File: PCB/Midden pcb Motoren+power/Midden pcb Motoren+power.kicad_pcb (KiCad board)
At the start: 2 copper layers, 232 parts, among them IC1 TB9051FTG, IC2 TB9051FTG, IC3 TB9051FTG, IC4 TB9051FTG, J4 Conn_01x08_Socket, J5 Conn_01x03_Socket, J6 Conn_01x08_Socket, J7 Conn_01x08_Pin, J8 Conn_01x03_Pin, SW10 SW_DIP_x04, SW5 SW_DIP_x03, SW6 SW_DPST_x2, SW7 SW_DIP_x04, SW8 SW_DIP_x04, SW9 SW_DIP_x04, U10 FT232RL, U11 ATmega328P-M, U12 ATmega328P-M, U13 FT232RL, U14 FT232RL, U6 ATmega328P-M, U7 ATmega328P-M, U9 FT232RL

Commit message: M1 is af
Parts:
- removed J5: Conn_01x03_Socket, Connector_JST:JST_EH_S3B-EH_1x03_P2.50mm_Horizontal
- removed J8: Conn_01x03_Pin, Connector_JST:JST_EH_S3B-EH_1x03_P2.50mm_Horizontal
- added J1: Conn_01x04_Pin, Connector_JST:JST_EH_S4B-EH_1x04_P2.50mm_Horizontal, F.Cu at (156.1, 132.2)
- added J2: Conn_01x04_Socket, Connector_JST:JST_EH_S4B-EH_1x04_P2.50mm_Horizontal, F.Cu at (98.5, 94.6)
- added J3: Conn_01x08_Socket, Connector_JST:JST_EH_S8B-EH_1x08_P2.50mm_Horizontal, F.Cu at (156.0, 145.8)
- C106, C83, C85, C86, C87, C97, C98, R101, R104, R109, R110, R111, R119, R120, R169, R170, R171, R172, R173, R174, R175, R176, R177, R205, R206, R207, R219, R220, R94, R95, R96, U6, U9: moved to B.Cu
- moved SW10 179.3 mm to (78.8, 118.8), turned to 120 degrees
- moved C98 156.8 mm to (125.3, 68.0)
- moved C97 156.7 mm to (125.3, 67.3)
- moved SW9 155.6 mm to (90.1, 112.2), turned to 120 degrees
- moved C87 151.1 mm to (125.5, 66.1), turned to 180 degrees
- moved C86 151.0 mm to (125.5, 65.4), turned to 180 degrees
- moved C85 151.0 mm to (125.5, 64.6)
- moved R219 147.4 mm to (115.3, 67.0)
- moved U6 146.3 mm to (121.2, 65.6), turned to 180 degrees
- moved R220 146.3 mm to (115.8, 64.0)
- moved M4 146.0 mm to (73.3, 127.1), turned to 30 degrees
- moved R170 132.8 mm to (118.1, 71.0), turned to 90 degrees
- moved R169 131.8 mm to (119.6, 70.9), turned to 90 degrees
- moved R171 131.4 mm to (117.7, 60.7), turned to -90 degrees
- moved R205 130.9 mm to (129.4, 81.8)
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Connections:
- net /12V renamed +12V
- 3V1 pad 1: GND -> /3V3
- 5V1 pad 1: GND -> /5V
- J6 pad 1: GND -> unconnected-(J6-Pin_1-Pad1)
- J6 pad 2: GND -> unconnected-(J6-Pin_2-Pad2)
- J6 pad 3: GND -> /SCL
- J6 pad 4: GND -> /SDA
- J6 pad 5: GND -> /LED
- J6 pad 6: GND -> /5V
- J6 pad 8: GND -> /3V3
- JP28 pad 2: GND -> /SCL
- JP29 pad 2: GND -> /SDA
- R125 pad 2: GND -> /SDA
- R126 pad 2: GND -> /SCL
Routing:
- net +5V: track 0.00 -> 93.0 mm, vias 0 -> 4
- net Net-(R95-Pad2): track 0.00 -> 50.6 mm, vias 0 -> 2
- net Net-(R94-Pad2): track 0.00 -> 47.7 mm, vias 0 -> 2
- net /tx-m1: track 0.00 -> 47.5 mm
- net /tx-m10: track 0.00 -> 44.0 mm, vias 0 -> 1
- net /out2-m1: track 0.00 -> 42.1 mm
- net /out1-m1: track 0.00 -> 41.4 mm
- net /rx-m1: track 0.00 -> 40.9 mm
- net /rx-m10: track 0.00 -> 36.7 mm, vias 0 -> 1
- net /enAM1: track 0.00 -> 23.0 mm, vias 0 -> 2
- net /ocm-m1: track 0.00 -> 21.4 mm, vias 0 -> 2
- net /encB-m1: track 0.00 -> 18.5 mm
- net /encA-m1: track 0.00 -> 17.8 mm, vias 0 -> 1
- net /pwm1-m1: track 0.00 -> 13.9 mm, vias 0 -> 3
- net /occ-m1: track 0.00 -> 13.7 mm, vias 0 -> 2
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- added copper zone on B.Cu, net GND
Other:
- board outline added: 153.6 x 125.2 mm

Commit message: v1
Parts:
- moved C115 10.9 mm to (212.5, 56.0)
- moved C133 10.9 mm to (216.8, 56.0)
- moved C91 10.9 mm to (273.7, 60.6)
- moved C92 10.9 mm to (273.7, 62.4)
- moved R114 10.9 mm to (225.5, 56.0)
- moved R146 10.9 mm to (234.2, 56.0)
- moved R162 10.9 mm to (238.6, 56.0)
- moved R178 10.9 mm to (242.9, 56.0)
- moved R194 10.9 mm to (247.3, 56.0)
- moved R210 10.9 mm to (251.6, 56.0)
- moved R98 10.9 mm to (221.2, 56.0)
- moved 5V1 10.9 mm to (196.3, 83.1)
- moved BT1 10.9 mm to (174.0, 112.7)
- moved BT2 10.9 mm to (168.1, 101.7)
- moved C100 10.9 mm to (276.5, 64.2)
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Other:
- board size 153.6 x 125.2 mm -> 148.1 x 115.8 mm

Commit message: m2
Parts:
- C100, C101, R106, R112, R113, R114, R187, R188, R189, R190, R191, R192, R193, R194, R195, R98, R99, U7: moved to B.Cu
- moved C100 152.9 mm to (127.4, 97.9)
- moved C101 152.7 mm to (127.4, 98.7)
- moved R188 142.8 mm to (118.4, 102.6), turned to 90 degrees
- moved R187 142.6 mm to (119.9, 102.6), turned to 90 degrees
- moved R189 138.0 mm to (117.7, 90.8), turned to -90 degrees
- moved R190 135.7 mm to (119.2, 90.8), turned to -90 degrees
- moved U7 135.7 mm to (122.6, 96.9), turned to 180 degrees
- moved R191 133.5 mm to (120.7, 90.8), turned to -90 degrees
- moved R195 129.1 mm to (125.9, 102.6), turned to 90 degrees
- moved R192 126.6 mm to (127.6, 92.5), turned to 180 degrees
- moved R193 126.3 mm to (127.6, 94.0), turned to 180 degrees
- moved R194 126.0 mm to (127.6, 95.6), turned to 180 degrees
- moved R106 117.0 mm to (122.2, 90.8), turned to 90 degrees
- moved R113 115.1 mm to (121.4, 102.6), turned to -90 degrees
- moved R112 113.5 mm to (124.4, 102.6), turned to -90 degrees
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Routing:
- net Net-(R98-Pad2): track 0.00 -> 50.6 mm
- net Net-(R99-Pad2): track 0.00 -> 48.1 mm
- net /out1-m3: track 0.00 -> 45.9 mm
- net /out2-m3: track 0.00 -> 27.5 mm
- net /encB-m3: track 0.00 -> 18.8 mm, vias 0 -> 1
- net /encA-m3: track 0.00 -> 17.6 mm, vias 0 -> 1
- net Net-(IC2-ENB): track 0.00 -> 17.6 mm, vias 0 -> 1
- net GND: track 0.00 -> 16.3 mm
- net Net-(IC2-OCC): track 0.00 -> 16.3 mm, vias 0 -> 1
- net Net-(IC2-EN): track 0.00 -> 12.0 mm
- net /pwm1-m3: track 0.00 -> 9.12 mm
- net Net-(U7-PC3): track 0.00 -> 5.20 mm
- net Net-(U7-PC4): track 0.00 -> 4.32 mm
- net Net-(U7-PD7): track 0.00 -> 4.01 mm
- net Net-(U7-PB4): track 0.00 -> 3.70 mm
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
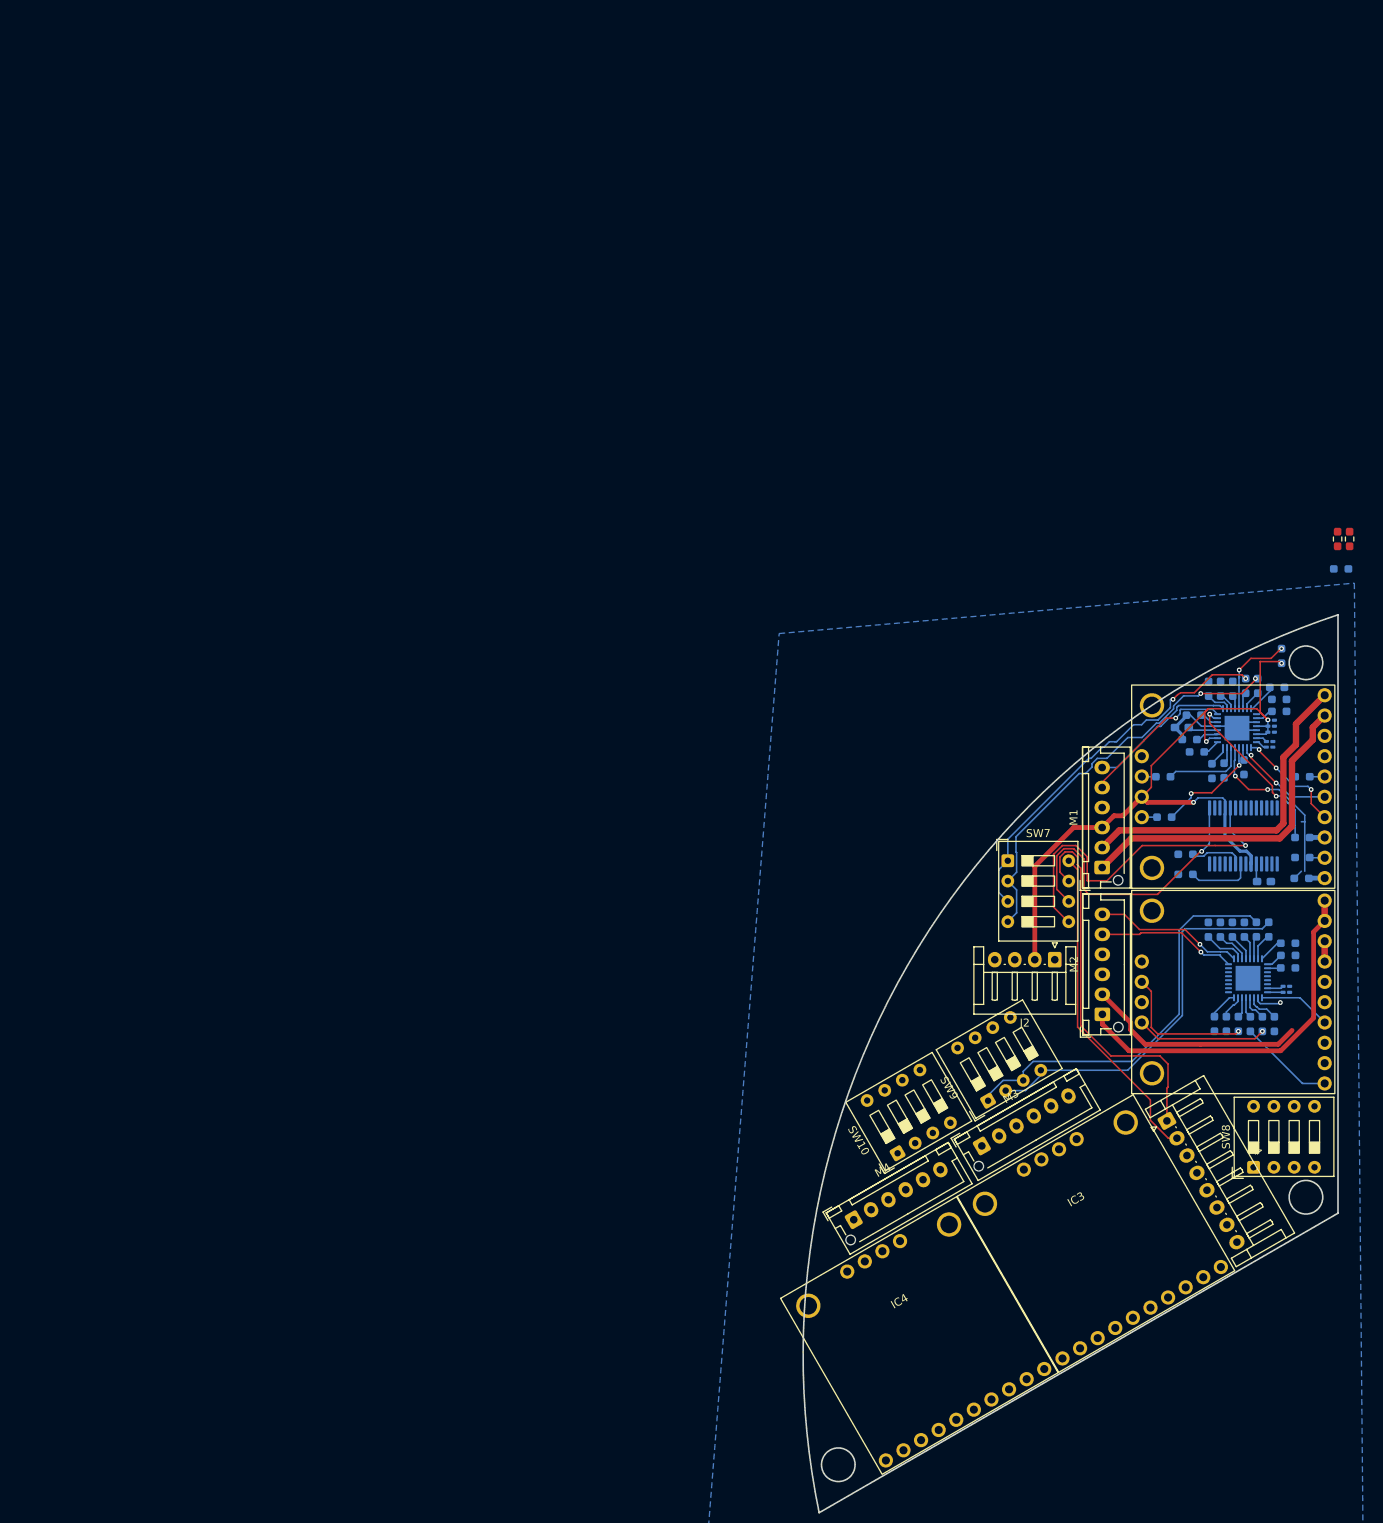
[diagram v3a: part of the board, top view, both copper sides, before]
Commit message: motor driver symbol changed
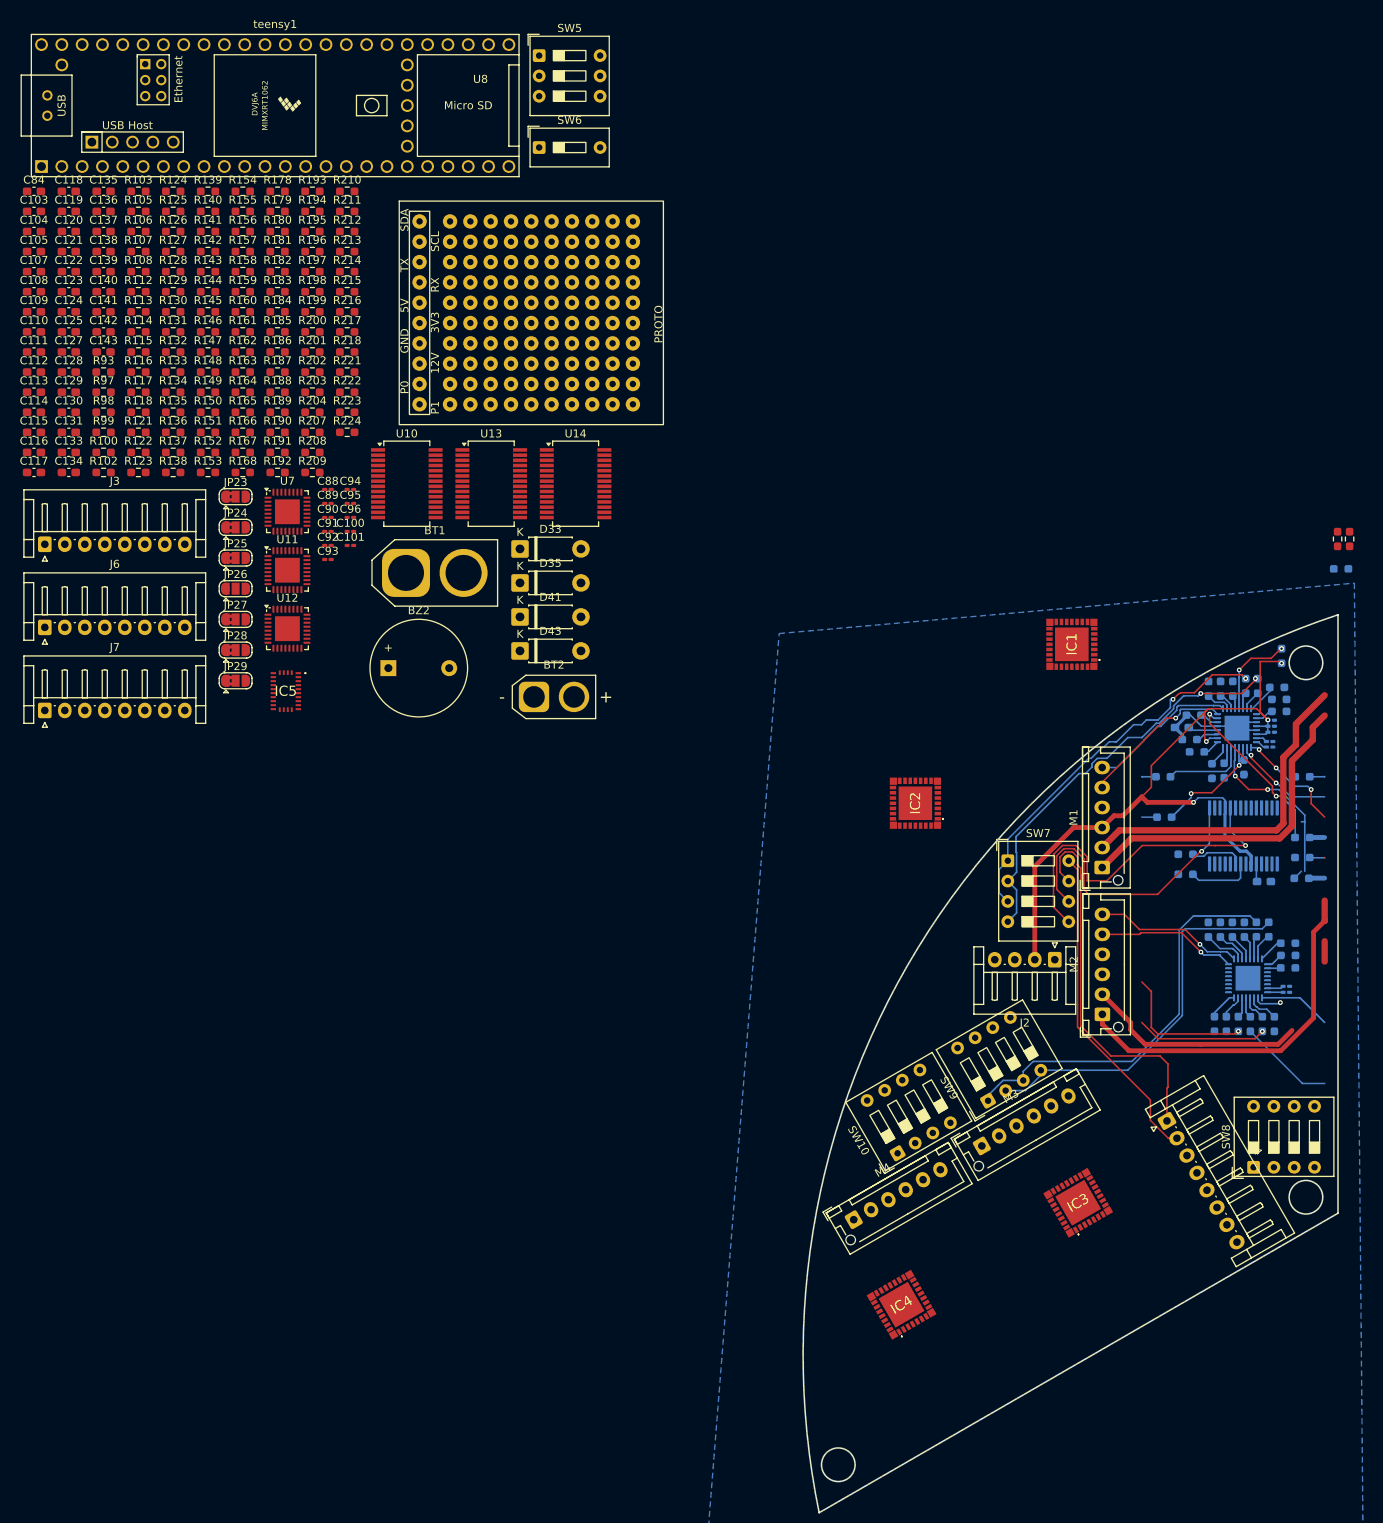
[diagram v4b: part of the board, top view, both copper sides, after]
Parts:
- added BT1: Battery, Connector_AMASS:AMASS_XT60-F_1x02_P7.20mm_Vertical, F.Cu at (17.4, 46.2)
- added BT2: Battery, Connector_AMASS:AMASS_XT30U-M_1x02_P5.0mm_Vertical, F.Cu at (33.4, 61.7)
- added BZ2: Buzzer, Buzzer_Beeper:Buzzer_12x9.5RM7.6, F.Cu at (15.2, 58.1)
- added C100: 20pF???, Capacitor_SMD:C_0201_0603Metric_Pad0.64x0.40mm_HandSolder, F.Cu at (10.4, 41.0)
- added C101: 20pF???, Capacitor_SMD:C_0201_0603Metric_Pad0.64x0.40mm_HandSolder, F.Cu at (10.4, 42.8)
- added C103: 47uF, Capacitor_SMD:C_0603_1608Metric_Pad1.08x0.95mm_HandSolder, F.Cu at (-29.1, 1.03)
- added C104: 47uF, Capacitor_SMD:C_0603_1608Metric_Pad1.08x0.95mm_HandSolder, F.Cu at (-29.1, 3.54)
- added C105: 0.1uF, Capacitor_SMD:C_0603_1608Metric_Pad1.08x0.95mm_HandSolder, F.Cu at (-29.1, 6.05)
- added C107: 0.1uF, Capacitor_SMD:C_0603_1608Metric_Pad1.08x0.95mm_HandSolder, F.Cu at (-29.1, 8.56)
- added C108: 0.1uF, Capacitor_SMD:C_0603_1608Metric_Pad1.08x0.95mm_HandSolder, F.Cu at (-29.1, 11.1)
- added C109: 100nF, Capacitor_SMD:C_0603_1608Metric_Pad1.08x0.95mm_HandSolder, F.Cu at (-29.1, 13.6)
- added C110: 0.1uF, Capacitor_SMD:C_0603_1608Metric_Pad1.08x0.95mm_HandSolder, F.Cu at (-29.1, 16.1)
- added C111: 100nF, Capacitor_SMD:C_0603_1608Metric_Pad1.08x0.95mm_HandSolder, F.Cu at (-29.1, 18.6)
- added C112: 4.7uF, Capacitor_SMD:C_0603_1608Metric_Pad1.08x0.95mm_HandSolder, F.Cu at (-29.1, 21.1)
- added C113: 1uF, Capacitor_SMD:C_0603_1608Metric_Pad1.08x0.95mm_HandSolder, F.Cu at (-29.1, 23.6)
- added C114: 1uF, Capacitor_SMD:C_0603_1608Metric_Pad1.08x0.95mm_HandSolder, F.Cu at (-29.1, 26.1)
- added C115: 100nF, Capacitor_SMD:C_0603_1608Metric_Pad1.08x0.95mm_HandSolder, F.Cu at (-29.1, 28.6)
- added C116: 0.1uF, Capacitor_SMD:C_0603_1608Metric_Pad1.08x0.95mm_HandSolder, F.Cu at (-29.1, 31.2)
- added C117: 4.7uF, Capacitor_SMD:C_0603_1608Metric_Pad1.08x0.95mm_HandSolder, F.Cu at (-29.1, 33.7)
- added C118: 4.7uF, Capacitor_SMD:C_0603_1608Metric_Pad1.08x0.95mm_HandSolder, F.Cu at (-24.8, -1.48)
- added C119: 1uF, Capacitor_SMD:C_0603_1608Metric_Pad1.08x0.95mm_HandSolder, F.Cu at (-24.8, 1.03)
- added C120: 1uF, Capacitor_SMD:C_0603_1608Metric_Pad1.08x0.95mm_HandSolder, F.Cu at (-24.8, 3.54)
- added C121: 0.47uF, Capacitor_SMD:C_0603_1608Metric_Pad1.08x0.95mm_HandSolder, F.Cu at (-24.8, 6.05)
- added C122: 0.1uF, Capacitor_SMD:C_0603_1608Metric_Pad1.08x0.95mm_HandSolder, F.Cu at (-24.8, 8.56)
- added C123: 20pF???, Capacitor_SMD:C_0603_1608Metric_Pad1.08x0.95mm_HandSolder, F.Cu at (-24.8, 11.1)
- added C124: 20pF???, Capacitor_SMD:C_0603_1608Metric_Pad1.08x0.95mm_HandSolder, F.Cu at (-24.8, 13.6)
- added C125: 4.7uF, Capacitor_SMD:C_0603_1608Metric_Pad1.08x0.95mm_HandSolder, F.Cu at (-24.8, 16.1)
- added C127: 0.47uF, Capacitor_SMD:C_0603_1608Metric_Pad1.08x0.95mm_HandSolder, F.Cu at (-24.8, 18.6)
- added C128: 47uF, Capacitor_SMD:C_0603_1608Metric_Pad1.08x0.95mm_HandSolder, F.Cu at (-24.8, 21.1)
- added C129: 0.1uF, Capacitor_SMD:C_0603_1608Metric_Pad1.08x0.95mm_HandSolder, F.Cu at (-24.8, 23.6)
- added C130: 20pF???, Capacitor_SMD:C_0603_1608Metric_Pad1.08x0.95mm_HandSolder, F.Cu at (-24.8, 26.1)
- added C131: 20pF???, Capacitor_SMD:C_0603_1608Metric_Pad1.08x0.95mm_HandSolder, F.Cu at (-24.8, 28.6)
- added C133: 100nF, Capacitor_SMD:C_0603_1608Metric_Pad1.08x0.95mm_HandSolder, F.Cu at (-24.8, 31.2)
- added C134: 0.1uF, Capacitor_SMD:C_0603_1608Metric_Pad1.08x0.95mm_HandSolder, F.Cu at (-24.8, 33.7)
- added C135: 0.1uF, Capacitor_SMD:C_0603_1608Metric_Pad1.08x0.95mm_HandSolder, F.Cu at (-20.4, -1.48)
- added C136: 47uF, Capacitor_SMD:C_0603_1608Metric_Pad1.08x0.95mm_HandSolder, F.Cu at (-20.4, 1.03)
- added C137: 0.1uF, Capacitor_SMD:C_0603_1608Metric_Pad1.08x0.95mm_HandSolder, F.Cu at (-20.4, 3.54)
- added C138: 0.1uF, Capacitor_SMD:C_0603_1608Metric_Pad1.08x0.95mm_HandSolder, F.Cu at (-20.4, 6.05)
- added C139: 0.1uF, Capacitor_SMD:C_0603_1608Metric_Pad1.08x0.95mm_HandSolder, F.Cu at (-20.4, 8.56)
- added C140: 100nF, Capacitor_SMD:C_0603_1608Metric_Pad1.08x0.95mm_HandSolder, F.Cu at (-20.4, 11.1)
- added C141: 0.1uF, Capacitor_SMD:C_0603_1608Metric_Pad1.08x0.95mm_HandSolder, F.Cu at (-20.4, 13.6)
- added C142: 22pF, Capacitor_SMD:C_0603_1608Metric_Pad1.08x0.95mm_HandSolder, F.Cu at (-20.4, 16.1)
- added C143: 22pF, Capacitor_SMD:C_0603_1608Metric_Pad1.08x0.95mm_HandSolder, F.Cu at (-20.4, 18.6)
- added C84: 100nF, Capacitor_SMD:C_0603_1608Metric_Pad1.08x0.95mm_HandSolder, F.Cu at (-29.1, -1.48)
- added C88: 4.7uF, Capacitor_SMD:C_0201_0603Metric_Pad0.64x0.40mm_HandSolder, F.Cu at (7.59, 35.8)
- added C89: 1uF, Capacitor_SMD:C_0201_0603Metric_Pad0.64x0.40mm_HandSolder, F.Cu at (7.59, 37.5)
- added C90: 1uF, Capacitor_SMD:C_0201_0603Metric_Pad0.64x0.40mm_HandSolder, F.Cu at (7.59, 39.3)
- added C91: 0.1uF, Capacitor_SMD:C_0201_0603Metric_Pad0.64x0.40mm_HandSolder, F.Cu at (7.59, 41.0)
- added C92: 0.1uF, Capacitor_SMD:C_0201_0603Metric_Pad0.64x0.40mm_HandSolder, F.Cu at (7.59, 42.8)
- added C93: 4.7uF, Capacitor_SMD:C_0201_0603Metric_Pad0.64x0.40mm_HandSolder, F.Cu at (7.59, 44.5)
- added C94: 0.47uF, Capacitor_SMD:C_0201_0603Metric_Pad0.64x0.40mm_HandSolder, F.Cu at (10.4, 35.8)
- added C95: 4.7uF, Capacitor_SMD:C_0201_0603Metric_Pad0.64x0.40mm_HandSolder, F.Cu at (10.4, 37.5)
- added C96: 0.47uF, Capacitor_SMD:C_0201_0603Metric_Pad0.64x0.40mm_HandSolder, F.Cu at (10.4, 39.3)
- added D33: 16.2v, Diode_THT:D_DO-41_SOD81_P7.62mm_Horizontal, F.Cu at (31.6, 43.2)
- added D35: 16.2v, Diode_THT:D_DO-41_SOD81_P7.62mm_Horizontal, F.Cu at (31.6, 47.5)
- added D41: 16.2v, Diode_THT:D_DO-41_SOD81_P7.62mm_Horizontal, F.Cu at (31.6, 51.7)
- added D43: 16.2v, Diode_THT:D_DO-41_SOD81_P7.62mm_Horizontal, F.Cu at (31.6, 56.0)
- added IC5: BNO086, SamacSys_Parts:BNO086, F.Cu at (2.33, 61.0)
- added J3: Conn_01x08_Socket, Connector_JST:JST_EH_S8B-EH_1x08_P2.50mm_Horizontal, F.Cu at (-27.8, 42.6)
- added J6: Conn_01x08_Socket, Connector_JST:JST_EH_S8B-EH_1x08_P2.50mm_Horizontal, F.Cu at (-27.8, 53.0)
- added J7: Conn_01x08_Pin, Connector_JST:JST_EH_S8B-EH_1x08_P2.50mm_Horizontal, F.Cu at (-27.8, 63.4)
- added JP23: SolderJumper_3_Bridged12, Jumper:SolderJumper-3_P1.3mm_Bridged2Bar12_RoundedPad1.0x1.5mm, F.Cu at (-3.95, 36.7)
- added JP24: SolderJumper_3_Bridged123, Jumper:SolderJumper-3_P1.3mm_Bridged2Bar12_RoundedPad1.0x1.5mm, F.Cu at (-3.95, 40.5)
- added JP25: SolderJumper_3_Bridged12, Jumper:SolderJumper-3_P1.3mm_Bridged2Bar12_RoundedPad1.0x1.5mm, F.Cu at (-3.95, 44.4)
- added JP26: SolderJumper_3_Bridged12, Jumper:SolderJumper-3_P1.3mm_Open_RoundedPad1.0x1.5mm, F.Cu at (-3.95, 48.2)
- added JP27: SolderJumper_2_Open, Jumper:SolderJumper-3_P1.3mm_Bridged2Bar12_RoundedPad1.0x1.5mm, F.Cu at (-3.95, 52.0)
- added JP28: SolderJumper_2_Bridged, Jumper:SolderJumper-3_P1.3mm_Bridged2Bar12_RoundedPad1.0x1.5mm, F.Cu at (-3.95, 55.9)
- added JP29: SolderJumper_2_Bridged, Jumper:SolderJumper-3_P1.3mm_Bridged2Bar12_RoundedPad1.0x1.5mm, F.Cu at (-3.95, 59.7)
- added R100: 100K, Resistor_SMD:R_0603_1608Metric_Pad0.98x0.95mm_HandSolder, F.Cu at (-20.4, 31.2)
- added R102: 220, Resistor_SMD:R_0603_1608Metric_Pad0.98x0.95mm_HandSolder, F.Cu at (-20.4, 33.7)
- added R103: 1K, Resistor_SMD:R_0603_1608Metric_Pad0.98x0.95mm_HandSolder, F.Cu at (-16.1, -1.48)
- added R105: 100K, Resistor_SMD:R_0603_1608Metric_Pad0.98x0.95mm_HandSolder, F.Cu at (-16.1, 1.03)
- added R106: 1K, Resistor_SMD:R_0603_1608Metric_Pad0.98x0.95mm_HandSolder, F.Cu at (-16.1, 3.54)
- added R107: 220, Resistor_SMD:R_0603_1608Metric_Pad0.98x0.95mm_HandSolder, F.Cu at (-16.1, 6.05)
- added R108: 1K, Resistor_SMD:R_0603_1608Metric_Pad0.98x0.95mm_HandSolder, F.Cu at (-16.1, 8.56)
- added R112: 1K, Resistor_SMD:R_0603_1608Metric_Pad0.98x0.95mm_HandSolder, F.Cu at (-16.1, 11.1)
- added R113: 1K, Resistor_SMD:R_0603_1608Metric_Pad0.98x0.95mm_HandSolder, F.Cu at (-16.1, 13.6)
- added R114: 1K, Resistor_SMD:R_0603_1608Metric_Pad0.98x0.95mm_HandSolder, F.Cu at (-16.1, 16.1)
- added R115: 10K, Resistor_SMD:R_0603_1608Metric_Pad0.98x0.95mm_HandSolder, F.Cu at (-16.1, 18.6)
- added R116: 220, Resistor_SMD:R_0603_1608Metric_Pad0.98x0.95mm_HandSolder, F.Cu at (-16.1, 21.1)
- added R117: 10K, Resistor_SMD:R_0603_1608Metric_Pad0.98x0.95mm_HandSolder, F.Cu at (-16.1, 23.6)
- added R118: 220, Resistor_SMD:R_0603_1608Metric_Pad0.98x0.95mm_HandSolder, F.Cu at (-16.1, 26.1)
- added R121: 1K, Resistor_SMD:R_0603_1608Metric_Pad0.98x0.95mm_HandSolder, F.Cu at (-16.1, 28.6)
- added R122: 1K, Resistor_SMD:R_0603_1608Metric_Pad0.98x0.95mm_HandSolder, F.Cu at (-16.1, 31.2)
- added R123: 1K, Resistor_SMD:R_0603_1608Metric_Pad0.98x0.95mm_HandSolder, F.Cu at (-16.1, 33.7)
- added R124: 1K, Resistor_SMD:R_0603_1608Metric_Pad0.98x0.95mm_HandSolder, F.Cu at (-11.7, -1.48)
- added R125: 10K, Resistor_SMD:R_0603_1608Metric_Pad0.98x0.95mm_HandSolder, F.Cu at (-11.7, 1.03)
- added R126: 10K, Resistor_SMD:R_0603_1608Metric_Pad0.98x0.95mm_HandSolder, F.Cu at (-11.7, 3.54)
- added R127: 1, Resistor_SMD:R_0603_1608Metric_Pad0.98x0.95mm_HandSolder, F.Cu at (-11.7, 6.05)
- added R128: 1K, Resistor_SMD:R_0603_1608Metric_Pad0.98x0.95mm_HandSolder, F.Cu at (-11.7, 8.56)
- added R129: 1K, Resistor_SMD:R_0603_1608Metric_Pad0.98x0.95mm_HandSolder, F.Cu at (-11.7, 11.1)
- added R130: 1K, Resistor_SMD:R_0603_1608Metric_Pad0.98x0.95mm_HandSolder, F.Cu at (-11.7, 13.6)
- added R131: 100K, Resistor_SMD:R_0603_1608Metric_Pad0.98x0.95mm_HandSolder, F.Cu at (-11.7, 16.1)
- added R132: 1K, Resistor_SMD:R_0603_1608Metric_Pad0.98x0.95mm_HandSolder, F.Cu at (-11.7, 18.6)
- added R133: 220, Resistor_SMD:R_0603_1608Metric_Pad0.98x0.95mm_HandSolder, F.Cu at (-11.7, 21.1)
- added R134: 1K, Resistor_SMD:R_0603_1608Metric_Pad0.98x0.95mm_HandSolder, F.Cu at (-11.7, 23.6)
- added R135: 1, Resistor_SMD:R_0603_1608Metric_Pad0.98x0.95mm_HandSolder, F.Cu at (-11.7, 26.1)
- added R136: 1K, Resistor_SMD:R_0603_1608Metric_Pad0.98x0.95mm_HandSolder, F.Cu at (-11.7, 28.6)
- added R137: 1K, Resistor_SMD:R_0603_1608Metric_Pad0.98x0.95mm_HandSolder, F.Cu at (-11.7, 31.2)
- added R138: 1K, Resistor_SMD:R_0603_1608Metric_Pad0.98x0.95mm_HandSolder, F.Cu at (-11.7, 33.7)
- added R139: 1K, Resistor_SMD:R_0603_1608Metric_Pad0.98x0.95mm_HandSolder, F.Cu at (-7.40, -1.48)
- added R140: 1K, Resistor_SMD:R_0603_1608Metric_Pad0.98x0.95mm_HandSolder, F.Cu at (-7.40, 1.03)
- added R141: 1K, Resistor_SMD:R_0603_1608Metric_Pad0.98x0.95mm_HandSolder, F.Cu at (-7.40, 3.54)
- added R142: 100K, Resistor_SMD:R_0603_1608Metric_Pad0.98x0.95mm_HandSolder, F.Cu at (-7.40, 6.05)
- added R143: 1K, Resistor_SMD:R_0603_1608Metric_Pad0.98x0.95mm_HandSolder, F.Cu at (-7.40, 8.56)
- added R144: 220, Resistor_SMD:R_0603_1608Metric_Pad0.98x0.95mm_HandSolder, F.Cu at (-7.40, 11.1)
- added R145: 1K, Resistor_SMD:R_0603_1608Metric_Pad0.98x0.95mm_HandSolder, F.Cu at (-7.40, 13.6)
- added R146: 10K, Resistor_SMD:R_0603_1608Metric_Pad0.98x0.95mm_HandSolder, F.Cu at (-7.40, 16.1)
- added R147: 1K, Resistor_SMD:R_0603_1608Metric_Pad0.98x0.95mm_HandSolder, F.Cu at (-7.40, 18.6)
- added R148: 1K, Resistor_SMD:R_0603_1608Metric_Pad0.98x0.95mm_HandSolder, F.Cu at (-7.40, 21.1)
- added R149: 1K, Resistor_SMD:R_0603_1608Metric_Pad0.98x0.95mm_HandSolder, F.Cu at (-7.40, 23.6)
- added R150: 1K, Resistor_SMD:R_0603_1608Metric_Pad0.98x0.95mm_HandSolder, F.Cu at (-7.40, 26.1)
- added R151: 1K, Resistor_SMD:R_0603_1608Metric_Pad0.98x0.95mm_HandSolder, F.Cu at (-7.40, 28.6)
- added R152: 4.7K, Resistor_SMD:R_0603_1608Metric_Pad0.98x0.95mm_HandSolder, F.Cu at (-7.40, 31.2)
- added R153: 1K, Resistor_SMD:R_0603_1608Metric_Pad0.98x0.95mm_HandSolder, F.Cu at (-7.40, 33.7)
- added R154: 10K, Resistor_SMD:R_0603_1608Metric_Pad0.98x0.95mm_HandSolder, F.Cu at (-3.05, -1.48)
- added R155: 10K, Resistor_SMD:R_0603_1608Metric_Pad0.98x0.95mm_HandSolder, F.Cu at (-3.05, 1.03)
- added R156: 4.7K, Resistor_SMD:R_0603_1608Metric_Pad0.98x0.95mm_HandSolder, F.Cu at (-3.05, 3.54)
- added R157: 220, Resistor_SMD:R_0603_1608Metric_Pad0.98x0.95mm_HandSolder, F.Cu at (-3.05, 6.05)
- added R158: 1K, Resistor_SMD:R_0603_1608Metric_Pad0.98x0.95mm_HandSolder, F.Cu at (-3.05, 8.56)
- added R159: 1K, Resistor_SMD:R_0603_1608Metric_Pad0.98x0.95mm_HandSolder, F.Cu at (-3.05, 11.1)
- added R160: 1K, Resistor_SMD:R_0603_1608Metric_Pad0.98x0.95mm_HandSolder, F.Cu at (-3.05, 13.6)
- added R161: 2.2K, Resistor_SMD:R_0603_1608Metric_Pad0.98x0.95mm_HandSolder, F.Cu at (-3.05, 16.1)
- added R162: 10K, Resistor_SMD:R_0603_1608Metric_Pad0.98x0.95mm_HandSolder, F.Cu at (-3.05, 18.6)
- added R163: 220, Resistor_SMD:R_0603_1608Metric_Pad0.98x0.95mm_HandSolder, F.Cu at (-3.05, 21.1)
- added R164: 1K, Resistor_SMD:R_0603_1608Metric_Pad0.98x0.95mm_HandSolder, F.Cu at (-3.05, 23.6)
- added R165: 2.2K, Resistor_SMD:R_0603_1608Metric_Pad0.98x0.95mm_HandSolder, F.Cu at (-3.05, 26.1)
- added R166: 1K, Resistor_SMD:R_0603_1608Metric_Pad0.98x0.95mm_HandSolder, F.Cu at (-3.05, 28.6)
- added R167: 1K, Resistor_SMD:R_0603_1608Metric_Pad0.98x0.95mm_HandSolder, F.Cu at (-3.05, 31.2)
- added R168: 1K, Resistor_SMD:R_0603_1608Metric_Pad0.98x0.95mm_HandSolder, F.Cu at (-3.05, 33.7)
- added R178: 10K, Resistor_SMD:R_0603_1608Metric_Pad0.98x0.95mm_HandSolder, F.Cu at (1.30, -1.48)
- added R179: 10K, Resistor_SMD:R_0603_1608Metric_Pad0.98x0.95mm_HandSolder, F.Cu at (1.30, 1.03)
- added R180: 10K, Resistor_SMD:R_0603_1608Metric_Pad0.98x0.95mm_HandSolder, F.Cu at (1.30, 3.54)
- added R181: 10K, Resistor_SMD:R_0603_1608Metric_Pad0.98x0.95mm_HandSolder, F.Cu at (1.30, 6.05)
- added R182: 10K, Resistor_SMD:R_0603_1608Metric_Pad0.98x0.95mm_HandSolder, F.Cu at (1.30, 8.56)
- added R183: 10K, Resistor_SMD:R_0603_1608Metric_Pad0.98x0.95mm_HandSolder, F.Cu at (1.30, 11.1)
- added R184: 10K, Resistor_SMD:R_0603_1608Metric_Pad0.98x0.95mm_HandSolder, F.Cu at (1.30, 13.6)
- added R185: 10K, Resistor_SMD:R_0603_1608Metric_Pad0.98x0.95mm_HandSolder, F.Cu at (1.30, 16.1)
- added R186: 10K, Resistor_SMD:R_0603_1608Metric_Pad0.98x0.95mm_HandSolder, F.Cu at (1.30, 18.6)
- added R187: 10K, Resistor_SMD:R_0603_1608Metric_Pad0.98x0.95mm_HandSolder, F.Cu at (1.30, 21.1)
- added R188: 10K, Resistor_SMD:R_0603_1608Metric_Pad0.98x0.95mm_HandSolder, F.Cu at (1.30, 23.6)
- added R189: 10K, Resistor_SMD:R_0603_1608Metric_Pad0.98x0.95mm_HandSolder, F.Cu at (1.30, 26.1)
- added R190: 10K, Resistor_SMD:R_0603_1608Metric_Pad0.98x0.95mm_HandSolder, F.Cu at (1.30, 28.6)
- added R191: 10K, Resistor_SMD:R_0603_1608Metric_Pad0.98x0.95mm_HandSolder, F.Cu at (1.30, 31.2)
- added R192: 10K, Resistor_SMD:R_0603_1608Metric_Pad0.98x0.95mm_HandSolder, F.Cu at (1.30, 33.7)
- added R193: 10K, Resistor_SMD:R_0603_1608Metric_Pad0.98x0.95mm_HandSolder, F.Cu at (5.65, -1.48)
- added R194: 10K, Resistor_SMD:R_0603_1608Metric_Pad0.98x0.95mm_HandSolder, F.Cu at (5.65, 1.03)
- added R195: 10K, Resistor_SMD:R_0603_1608Metric_Pad0.98x0.95mm_HandSolder, F.Cu at (5.65, 3.54)
- added R196: 10K, Resistor_SMD:R_0603_1608Metric_Pad0.98x0.95mm_HandSolder, F.Cu at (5.65, 6.05)
- added R197: 10K, Resistor_SMD:R_0603_1608Metric_Pad0.98x0.95mm_HandSolder, F.Cu at (5.65, 8.56)
- added R198: 10K, Resistor_SMD:R_0603_1608Metric_Pad0.98x0.95mm_HandSolder, F.Cu at (5.65, 11.1)
- added R199: 10K, Resistor_SMD:R_0603_1608Metric_Pad0.98x0.95mm_HandSolder, F.Cu at (5.65, 13.6)
- added R200: 10K, Resistor_SMD:R_0603_1608Metric_Pad0.98x0.95mm_HandSolder, F.Cu at (5.65, 16.1)
- added R201: 10K, Resistor_SMD:R_0603_1608Metric_Pad0.98x0.95mm_HandSolder, F.Cu at (5.65, 18.6)
- added R202: 10K, Resistor_SMD:R_0603_1608Metric_Pad0.98x0.95mm_HandSolder, F.Cu at (5.65, 21.1)
- added R203: 10K, Resistor_SMD:R_0603_1608Metric_Pad0.98x0.95mm_HandSolder, F.Cu at (5.65, 23.6)
- added R204: 10K, Resistor_SMD:R_0603_1608Metric_Pad0.98x0.95mm_HandSolder, F.Cu at (5.65, 26.1)
- added R207: 10K, Resistor_SMD:R_0603_1608Metric_Pad0.98x0.95mm_HandSolder, F.Cu at (5.65, 28.6)
- added R208: 10K, Resistor_SMD:R_0603_1608Metric_Pad0.98x0.95mm_HandSolder, F.Cu at (5.65, 31.2)
- added R209: 10K, Resistor_SMD:R_0603_1608Metric_Pad0.98x0.95mm_HandSolder, F.Cu at (5.65, 33.7)
- added R210: 10K, Resistor_SMD:R_0603_1608Metric_Pad0.98x0.95mm_HandSolder, F.Cu at (10.0, -1.48)
- added R211: 10K, Resistor_SMD:R_0603_1608Metric_Pad0.98x0.95mm_HandSolder, F.Cu at (10.0, 1.03)
- added R212: 10K, Resistor_SMD:R_0603_1608Metric_Pad0.98x0.95mm_HandSolder, F.Cu at (10.0, 3.54)
- added R213: 10K, Resistor_SMD:R_0603_1608Metric_Pad0.98x0.95mm_HandSolder, F.Cu at (10.0, 6.05)
- added R214: 10K, Resistor_SMD:R_0603_1608Metric_Pad0.98x0.95mm_HandSolder, F.Cu at (10.0, 8.56)
- added R215: 10K, Resistor_SMD:R_0603_1608Metric_Pad0.98x0.95mm_HandSolder, F.Cu at (10.0, 11.1)
- added R216: 10K, Resistor_SMD:R_0603_1608Metric_Pad0.98x0.95mm_HandSolder, F.Cu at (10.0, 13.6)
- added R217: 10K, Resistor_SMD:R_0603_1608Metric_Pad0.98x0.95mm_HandSolder, F.Cu at (10.0, 16.1)
- added R218: 10K, Resistor_SMD:R_0603_1608Metric_Pad0.98x0.95mm_HandSolder, F.Cu at (10.0, 18.6)
- added R221: 10K, Resistor_SMD:R_0603_1608Metric_Pad0.98x0.95mm_HandSolder, F.Cu at (10.0, 21.1)
- added R222: 10K, Resistor_SMD:R_0603_1608Metric_Pad0.98x0.95mm_HandSolder, F.Cu at (10.0, 23.6)
- added R223: 10K, Resistor_SMD:R_0603_1608Metric_Pad0.98x0.95mm_HandSolder, F.Cu at (10.0, 26.1)
- added R224: 10K, Resistor_SMD:R_0603_1608Metric_Pad0.98x0.95mm_HandSolder, F.Cu at (10.0, 28.6)
- added R93: 1, Resistor_SMD:R_0603_1608Metric_Pad0.98x0.95mm_HandSolder, F.Cu at (-20.4, 21.1)
- added R97: 1, Resistor_SMD:R_0603_1608Metric_Pad0.98x0.95mm_HandSolder, F.Cu at (-20.4, 23.6)
- added R98: 1K, Resistor_SMD:R_0603_1608Metric_Pad0.98x0.95mm_HandSolder, F.Cu at (-20.4, 26.1)
- added R99: 1K, Resistor_SMD:R_0603_1608Metric_Pad0.98x0.95mm_HandSolder, F.Cu at (-20.4, 28.6)
- added SW5: SW_DIP_x03, Button_Switch_THT:SW_DIP_SPSTx03_Slide_9.78x9.8mm_W7.62mm_P2.54mm, F.Cu at (34.0, -18.4)
- added SW6: SW_DPST_x2, Button_Switch_THT:SW_DIP_SPSTx01_Slide_9.78x4.72mm_W7.62mm_P2.54mm, F.Cu at (34.0, -6.95)
- added U10: FT232RL, Package_SO:SSOP-28_5.3x10.2mm_P0.65mm, F.Cu at (17.5, 35.1)
- added U11: ATmega328P-M, Package_DFN_QFN:QFN-32-1EP_5x5mm_P0.5mm_EP3.1x3.1mm, F.Cu at (2.53, 45.9)
- added U12: ATmega328P-M, Package_DFN_QFN:QFN-32-1EP_5x5mm_P0.5mm_EP3.1x3.1mm, F.Cu at (2.53, 53.2)
- added U13: FT232RL, Package_SO:SSOP-28_5.3x10.2mm_P0.65mm, F.Cu at (28.0, 35.1)
- added U14: FT232RL, Package_SO:SSOP-28_5.3x10.2mm_P0.65mm, F.Cu at (38.6, 35.1)
- added U7: ATmega328P-M, Package_DFN_QFN:QFN-32-1EP_5x5mm_P0.5mm_EP3.1x3.1mm, F.Cu at (2.53, 38.6)
- added U8: ~, teensy.pretty-master:protoboard, F.Cu at (26.7, -2.79)
- added teensy1: Teensy4.1, teensy.pretty-master:Teensy41, F.Cu at (1.00, -12.2)
- IC1, IC2, IC3, IC4: footprint Lib:TB9051FTG -> SamacSys_Parts:TB9051FTG
- moved IC2 42.4 mm to (81.0, 75.0)
- moved IC1 23.7 mm to (100.6, 55.1)
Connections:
- J2 pad 2: +5V -> /5V
